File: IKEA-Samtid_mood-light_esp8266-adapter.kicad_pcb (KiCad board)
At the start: 2 copper layers, 17.5 x 17.8 mm, 11 parts, among them P1 ESP8266-01, P2 mood-light, U1 AMS1117-3.3

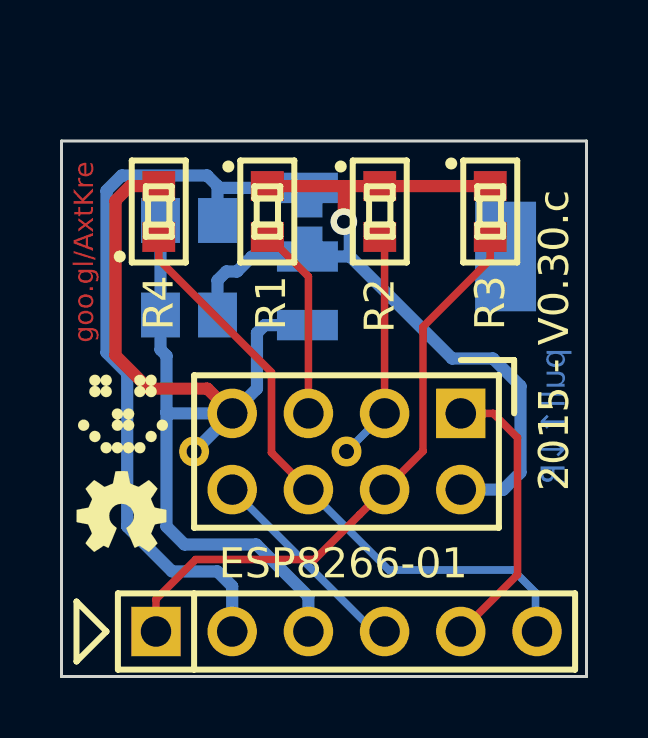
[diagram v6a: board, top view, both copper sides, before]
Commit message: ESP8266 adapter: played with trace length tuning a bit (just for fun).
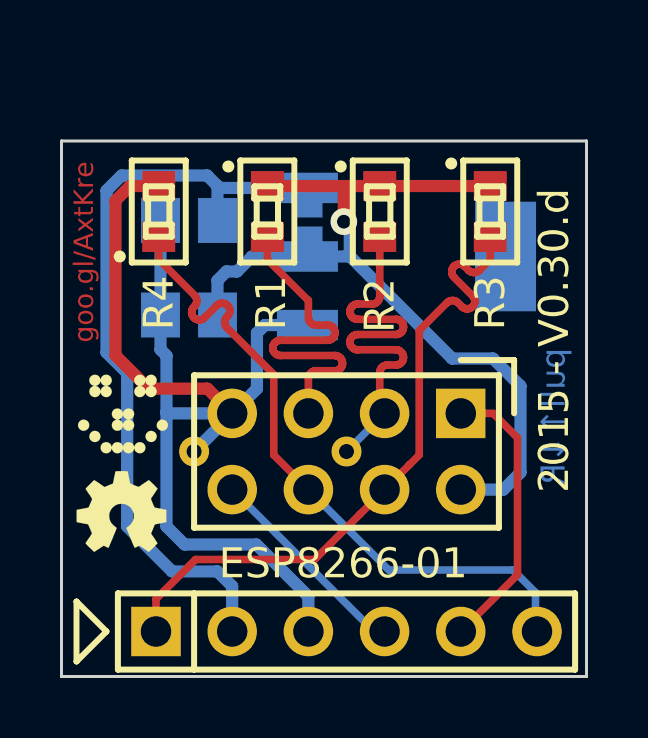
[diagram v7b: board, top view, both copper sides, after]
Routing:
- net Net-(P1-Pad3): track 7.74 -> 13.8 mm
- net Net-(P1-Pad5): track 6.48 -> 12.0 mm
- net /RST: track 20.1 -> 22.2 mm
- net /CH_PD: track 20.8 -> 22.3 mm
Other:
- board text added: "2015 - V0.30.d"
- board text removed: "2015 - V0.30.c"
